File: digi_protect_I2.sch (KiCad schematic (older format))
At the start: 5 parts

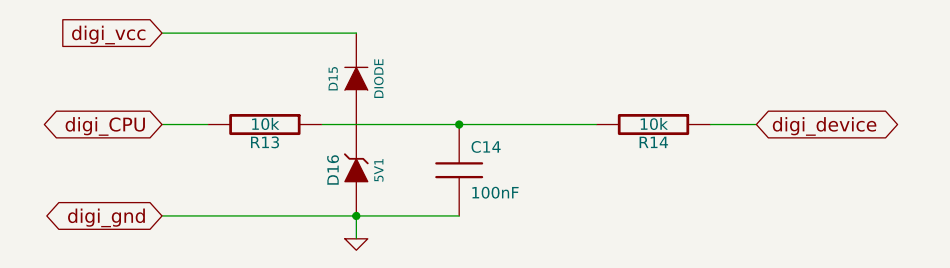
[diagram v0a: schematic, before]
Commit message: DFH mans up a bit. Perhaps usable for something at this point, like making trips to the local store ;)
I connected TA pins to sub circuits, fixed a number if items discussed in the DIYEFI forums. This is it's 21st version, so it was time for it to man up a bit, and become something potentially useful.

Signed-off-by: Jared Harvey <TortiseGIT@jaredharvey.com>
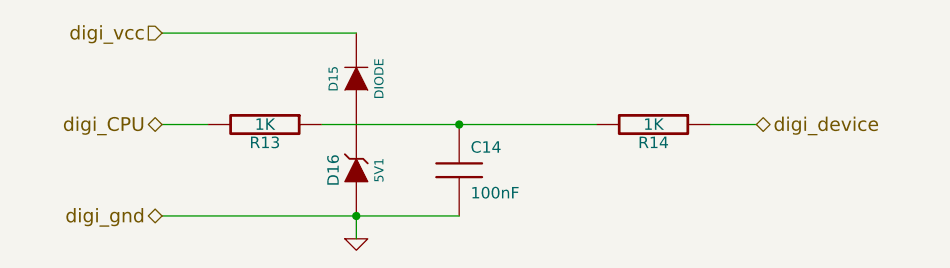
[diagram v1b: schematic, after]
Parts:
- C14: Field10 (none) -> Multilayer Ceramic; Field11 (none) -> other,more,stuff; Field4 (none) -> newark,39K8137; Field5 (none) -> vendor1, smd w hem; Field6 (none) -> vendor2, thru w hem; Field7 (none) -> vendor2, smd w hem; Field8 (none) -> 50,V; Field9 (none) -> 10,%
- D15: Field10 (none) -> x; Field11 (none) -> other,more,stuff; Field4 (none) -> newark,98K1092; Field5 (none) -> vendor1, smd w hem; Field6 (none) -> vendor2, thru w hem; Field7 (none) -> vendor2, smd w hem; Field8 (none) -> reverse,V; Field9 (none) -> current,A
- D16: Field10 (none) -> X; Field11 (none) -> other,more,stuff; Field4 (none) -> newark,18M3285; Field5 (none) -> vendor1, smd w hem; Field6 (none) -> vendor2, thru w hem; Field7 (none) -> vendor2, smd w hem; Field8 (none) -> 500,mW; Field9 (none) -> 20,mA
- R13, R14: value 10k -> 1K; TOL (none) -> 5%; W (none) -> 1/4W; construct (none) -> carbon film; misc (none) -> other,more,stuff; vend1,smd e hem (none) -> newark,52K9725; vend2, smd w hem (none) -> digi,CRCW08051K00JNEA; vend2, thru w hem (none) -> digi,OD102J-ND; vendor1, thru e hem (none) -> newark,65K2365
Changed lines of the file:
@@
-EESchema Schematic File Version 1
-LIBS:power,./freeEMS_lib,device,conn,linear,regul,74xx,cmos4000,adc-dac,memory,xilinx,special,microcontrollers,dsp,microchip,analog_switches,motorola,texas,intel,audio,interface,digital-audio,philips,display,cypress,siliconi,contrib,valves,./freeEMS_1.cache
-EELAYER 23  0
+EESchema Schematic File Version 2  date 9/10/2011 11:43:49 AM
+LIBS:power
+LIBS:freeEMS_lib
+LIBS:device
+LIBS:conn
+LIBS:linear
+LIBS:regul
+LIBS:74xx
+LIBS:cmos4000
+LIBS:adc-dac
+LIBS:memory
+LIBS:xilinx
+LIBS:special
+LIBS:microcontrollers
+LIBS:dsp
+LIBS:microchip
+LIBS:analog_switches
+LIBS:motorola
+LIBS:texas
+LIBS:intel
+LIBS:audio
+LIBS:interface
+LIBS:digital-audio
+LIBS:philips
+LIBS:display
+LIBS:cypress
+LIBS:siliconi
+LIBS:contrib
+LIBS:valves
+LIBS:freeEMS_1-cache
+EELAYER 25  0
 EELAYER END
 $Descr A4 11700 8267
+encoding utf-8
 Sheet 5 41
-Title "freeEMS 1.0"
-Date "15 nov 2008"
-Rev "A.20"
-Comp "diyefi.org"
+Title "DFH for freeEMS"
+Date "10 sep 2011"
+Rev "A.21"
+Comp "FreeEMS.org"
 Comment1 "digi_protect.sch"
 Comment2 ""
@@
 $Comp
 L R R14
-U 1 1 489B944C
+U 1 1 4E6B7027
 P 4100 1750
-F 0 "R14" V 4180 1750 50  0000 C C
-F 1 "10k" V 4100 1750 50  0000 C C
-F 2 "R4-SM0805" V 4280 1850 60  0001 C C
-F 4 "newark,38K0328" V 1130 2600 60  0001 C C
-F 5 "vendor1, smd w hem" V 1130 2600 60  0001 C C
-F 6 "vendor2, thru w hem" V 1130 2600 60  0001 C C
-F 7 "vendor2, smd w hem" V 1130 2600 60  0001 C C
-F 8 "250,mW" V 1130 2600 60  0001 C C
-F 9 "5,%" V 1130 2600 60  0001 C C
-F 10 "Carbon Film" V 1130 2600 60  0001 C C
-F 11 "other,more,stuff" V 1130 2600 60  0001 C C
+F 0 "R14" V 4180 1750 50  0000 C CNN
+F 1 "1K" V 4100 1750 50  0000 C CNN
+F 2 "R4-SM0805" V 1130 2600 60  0001 C CNN
+F 4 "newark,65K2365" V 1130 2600 60  0001 C CNN "vendor1, thru e hem"
+F 5 "newark,52K9725" V 1130 2600 60  0001 C CNN "vend1,smd e hem"
+F 6 "digi,OD102J-ND" V 1130 2600 60  0001 C CNN "vend2, thru w hem"
+F 7 "digi,CRCW08051K00JNEA" V 1130 2600 60  0001 C CNN "vend2, smd w hem"
+F 8 "1/4W" V 1130 2600 60  0001 C CNN "W"
+F 9 "5%" V 1130 2600 60  0001 C CNN "TOL"
+F 10 "carbon film" V 1130 2600 60  0001 C CNN "construct"
+F 11 "other,more,stuff" V 1130 2600 60  0001 C CNN "misc"
 	1    4100 1750
 	0    1    1    0
@@
 $Comp
 L DIODE D15
-U 1 1 489B937D
+U 1 1 4E6B7016
 P 2800 1550
-F 0 "D15" H 2800 1650 40  0000 C C
-F 1 "DIODE" H 2800 1450 40  0000 C C
-F 2 "D4-SMB" V 1130 2600 60  0001 C C
-F 4 "newark,98K1092" V 1130 2600 60  0001 C C
-F 5 "vendor1, smd w hem" V 1130 2600 60  0001 C C
-F 6 "vendor2, thru w hem" V 1130 2600 60  0001 C C
-F 7 "vendor2, smd w hem" V 1130 2600 60  0001 C C
-F 8 "reverse,V" V 1130 2600 60  0001 C C
-F 9 "current,A" V 1130 2600 60  0001 C C
-F 10 "x" V 1130 2600 60  0001 C C
-F 11 "other,more,stuff" V 1130 2600 60  0001 C C
+F 0 "D15" H 2800 1650 40  0000 C CNN
+F 1 "DIODE" H 2800 1450 40  0000 C CNN
+F 2 "D4-SMB" V 1130 2600 60  0001 C CNN
+F 4 "newark,98K1092" V 1130 2600 60  0001 C CNN "Field4"
+F 5 "vendor1, smd w hem" V 1130 2600 60  0001 C CNN "Field5"
+F 6 "vendor2, thru w hem" V 1130 2600 60  0001 C CNN "Field6"
+F 7 "vendor2, smd w hem" V 1130 2600 60  0001 C CNN "Field7"
+F 8 "reverse,V" V 1130 2600 60  0001 C CNN "Field8"
+F 9 "current,A" V 1130 2600 60  0001 C CNN "Field9"
+F 10 "x" V 1130 2600 60  0001 C CNN "Field10"
+F 11 "other,more,stuff" V 1130 2600 60  0001 C CNN "Field11"
 	1    2800 1550
 	0    -1   -1   0
 $EndComp
-Text GLabel 1950 1350 0    60   Input
+Text HLabel 1950 1350 0    60   Input ~ 0
 digi_vcc
 $Comp
 L ZENER D16
-U 1 1 486F8DB9
+U 1 1 4E6B6FB9
 P 2800 1950
-F 0 "D16" H 2800 2050 50  0000 C C
-F 1 "5V1" H 2800 1850 40  0000 C C
-F 2 "D4-SMB" V 1130 2600 60  0001 C C
-F 4 "newark,18M3285" V 1130 2600 60  0001 C C
-F 5 "vendor1, smd w hem" V 1130 2600 60  0001 C C
-F 6 "vendor2, thru w hem" V 1130 2600 60  0001 C C
-F 7 "vendor2, smd w hem" V 1130 2600 60  0001 C C
-F 8 "500,mW" V 1130 2600 60  0001 C C
-F 9 "20,mA" V 1130 2600 60  0001 C C
-F 10 "X" V 1130 2600 60  0001 C C
-F 11 "other,more,stuff" V 1130 2600 60  0001 C C
+F 0 "D16" H 2800 2050 50  0000 C CNN
+F 1 "5V1" H 2800 1850 40  0000 C CNN
+F 2 "D4-SMB" V 1130 2600 60  0001 C CNN
+F 4 "newark,18M3285" V 1130 2600 60  0001 C CNN "Field4"
+F 5 "vendor1, smd w hem" V 1130 2600 60  0001 C CNN "Field5"
+F 6 "vendor2, thru w hem" V 1130 2600 60  0001 C CNN "Field6"
+F 7 "vendor2, smd w hem" V 1130 2600 60  0001 C CNN "Field7"
+F 8 "500,mW" V 1130 2600 60  0001 C CNN "Field8"
+F 9 "20,mA" V 1130 2600 60  0001 C CNN "Field9"
+F 10 "X" V 1130 2600 60  0001 C CNN "Field10"
+F 11 "other,more,stuff" V 1130 2600 60  0001 C CNN "Field11"
 	1    2800 1950
 	0    -1   -1   0
@@
 $Comp
 L R R13
-U 1 1 486F8D89
+U 1 1 4E6B6FB1
 P 2400 1750
-F 0 "R13" V 2480 1750 50  0000 C C
-F 1 "10k" V 2400 1750 50  0000 C C
-F 2 "R4-SM0805" V 2580 1850 60  0001 C C
-F 4 "newark,38K0328" V 1130 2600 60  0001 C C
-F 5 "vendor1, smd w hem" V 1130 2600 60  0001 C C
-F 6 "vendor2, thru w hem" V 1130 2600 60  0001 C C
-F 7 "vendor2, smd w hem" V 1130 2600 60  0001 C C
-F 8 "250,mW" V 1130 2600 60  0001 C C
-F 9 "5,%" V 1130 2600 60  0001 C C
-F 10 "Carbon Film" V 1130 2600 60  0001 C C
-F 11 "other,more,stuff" V 1130 2600 60  0001 C C
+F 0 "R13" V 2480 1750 50  0000 C CNN
+F 1 "1K" V 2400 1750 50  0000 C CNN
+F 2 "R4-SM0805" V 1130 2600 60  0001 C CNN
+F 4 "newark,65K2365" V 1130 2600 60  0001 C CNN "vendor1, thru e hem"
+F 5 "newark,52K9725" V 1130 2600 60  0001 C CNN "vend1,smd e hem"
+F 6 "digi,OD102J-ND" V 1130 2600 60  0001 C CNN "vend2, thru w hem"
+F 7 "digi,CRCW08051K00JNEA" V 1130 2600 60  0001 C CNN "vend2, smd w hem"
+F 8 "1/4W" V 1130 2600 60  0001 C CNN "W"
+F 9 "5%" V 1130 2600 60  0001 C CNN "TOL"
+F 10 "carbon film" V 1130 2600 60  0001 C CNN "construct"
+F 11 "other,more,stuff" V 1130 2600 60  0001 C CNN "misc"
 	1    2400 1750
 	0    1    1    0
@@
 $Comp
 L C C14
-U 1 1 486F8D85
+U 1 1 4E6B6FA0
 P 3250 1950
-F 0 "C14" H 3300 2050 50  0000 L C
-F 1 "100nF" H 3300 1850 50  0000 L C
-F 2 "C1V7" V 1130 2600 60  0001 C C
-F 4 "newark,39K8137" V 1130 2600 60  0001 C C
-F 5 "vendor1, smd w hem" V 1130 2600 60  0001 C C
-F 6 "vendor2, thru w hem" V 1130 2600 60  0001 C C
-F 7 "vendor2, smd w hem" V 1130 2600 60  0001 C C
-F 8 "50,V" V 1130 2600 60  0001 C C
-F 9 "10,%" V 1130 2600 60  0001 C C
-F 10 "Multilayer Ceramic" V 1130 2600 60  0001 C C
-F 11 "other,more,stuff" V 1130 2600 60  0001 C C
+F 0 "C14" H 3300 2050 50  0000 L CNN
+F 1 "100nF" H 3300 1850 50  0000 L CNN
+F 2 "C1V7" V 1130 2600 60  0001 C CNN
+F 4 "newark,39K8137" V 1130 2600 60  0001 C CNN "Field4"
+F 5 "vendor1, smd w hem" V 1130 2600 60  0001 C CNN "Field5"
+F 6 "vendor2, thru w hem" V 1130 2600 60  0001 C CNN "Field6"
+F 7 "vendor2, smd w hem" V 1130 2600 60  0001 C CNN "Field7"
+F 8 "50,V" V 1130 2600 60  0001 C CNN "Field8"
+F 9 "10,%" V 1130 2600 60  0001 C CNN "Field9"
+F 10 "Multilayer Ceramic" V 1130 2600 60  0001 C CNN "Field10"
+F 11 "other,more,stuff" V 1130 2600 60  0001 C CNN "Field11"
 	1    3250 1950
 	1    0    0    -1
@@
 $Comp
 L GND #PWR026
-U 1 1 486F8D7E
+U 1 1 4E6B6F9C
 P 2800 2250
-F 0 "#PWR026" H 2800 2250 30  0001 C C
-F 1 "GND" H 2800 2180 30  0001 C C
+F 0 "#PWR026" H 2800 2250 30  0001 C CNN
+F 1 "GND" H 2800 2180 30  0001 C CNN
 	1    2800 2250
 	1    0    0    -1
 $EndComp
-Text GLabel 1950 2150 0    60   BiDi
+Text HLabel 1950 2150 0    60   BiDi ~ 0
 digi_gnd
-Text GLabel 1950 1750 0    60   BiDi
+Text HLabel 1950 1750 0    60   BiDi ~ 0
 digi_CPU
-Text GLabel 4550 1750 2    60   BiDi
+Text HLabel 4550 1750 2    60   BiDi ~ 0
 digi_device
 $EndSCHEMATC
